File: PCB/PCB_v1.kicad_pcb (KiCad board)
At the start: 2 copper layers, 0 parts

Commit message: Accelerometer Footprint
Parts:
- added J1: Accelerometer, Stuffed Crust:Accelerometer, F.Cu at (179.4, 71.4)
- added J2: Flysky FS2A Receiver, Stuffed Crust:Flysky_FS2A_Receiver, F.Cu at (179.6, 94.1)
- added J3: DC-DC, Stuffed Crust:DC_DC, F.Cu at (137.0, 68.5)
- added J4: Battery Left, Stuffed Crust:Battery_or_LED, F.Cu at (98.2, 75.7)
- added J5: Battery Right, Stuffed Crust:Battery_or_LED, F.Cu at (212.0, 69.9)
- added J6: ESC Left, Stuffed Crust:ESC, F.Cu at (111.0, 91.5)
- added J7: ESC Right, Stuffed Crust:ESC, F.Cu at (214.0, 89.5)
- added J8: LED, Stuffed Crust:Battery_or_LED, F.Cu at (179.3, 61.3)
- added U1: Teensy4.0, Teensy:Teensy40, F.Cu at (164.1, 79.6)

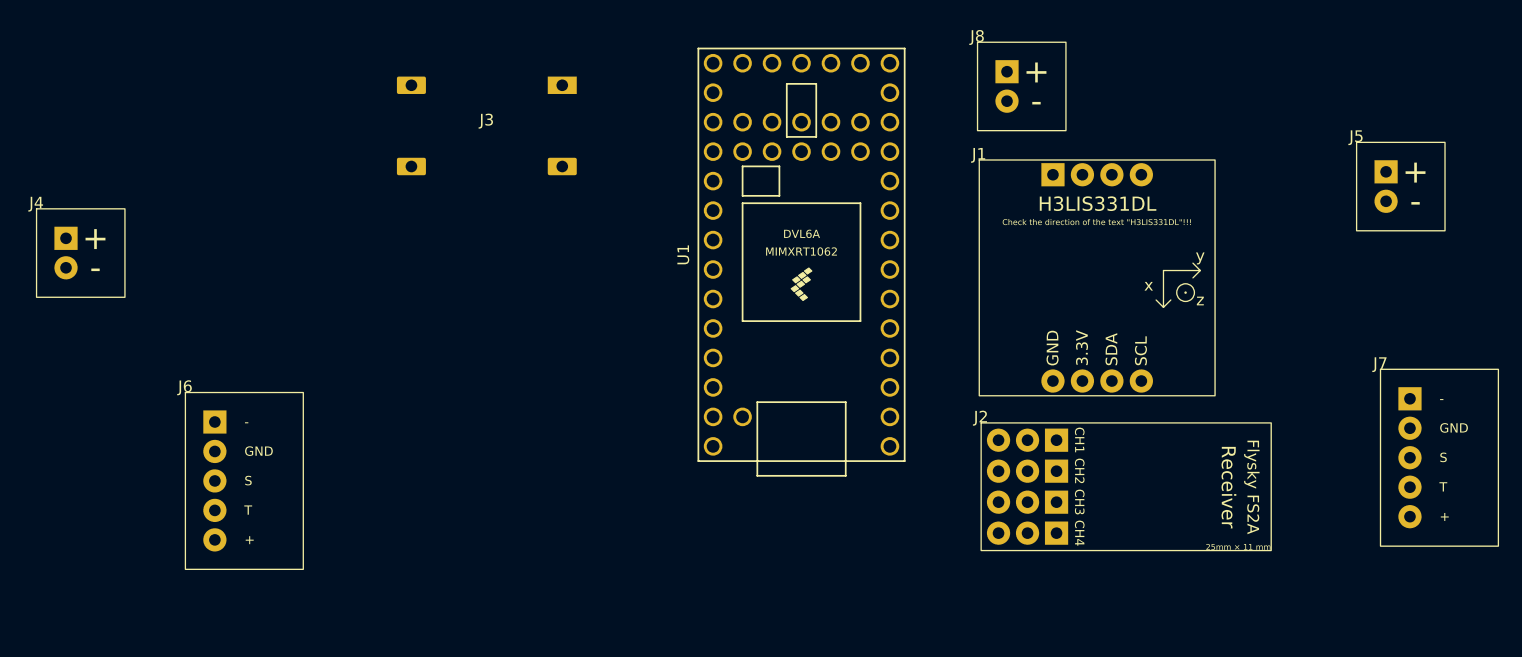
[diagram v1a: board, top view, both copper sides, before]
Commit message: Fix the layer issue in ESC footprint
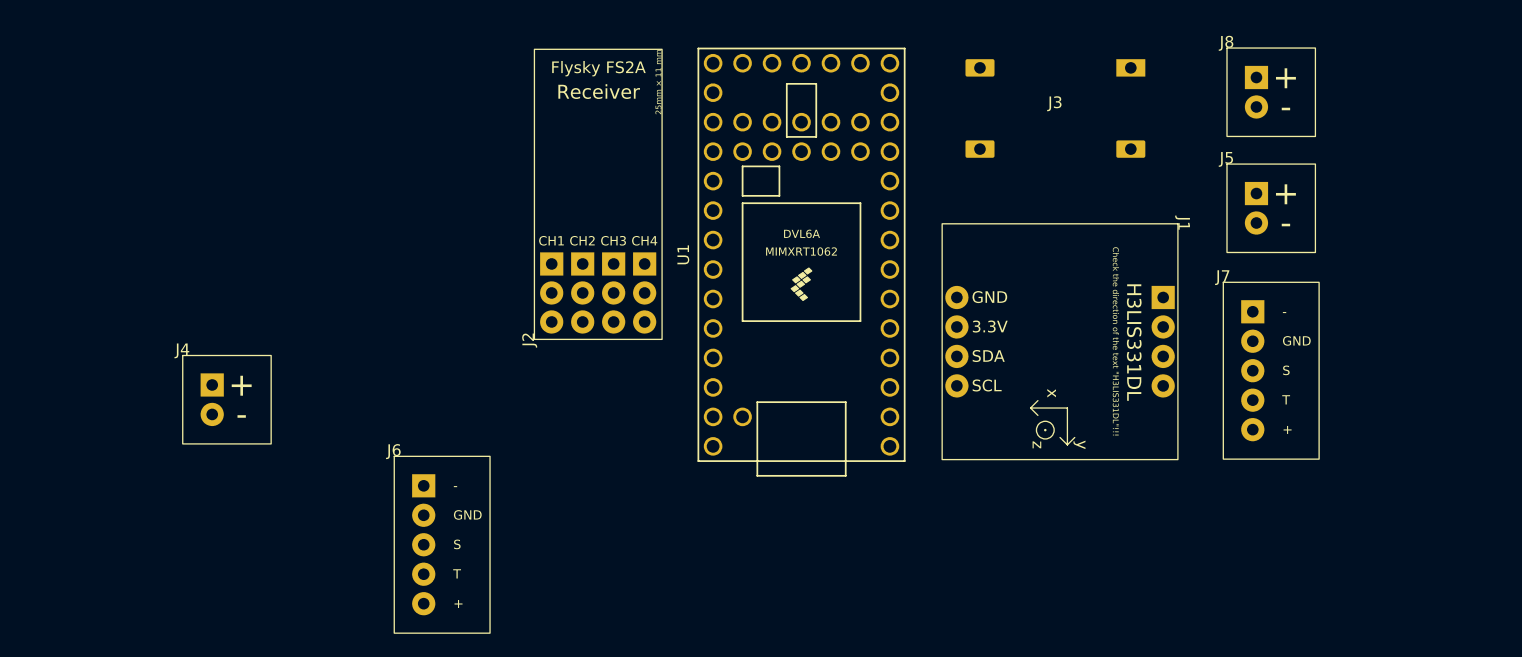
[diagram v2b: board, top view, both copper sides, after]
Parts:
- moved J3 49.0 mm to (186.0, 67.0)
- moved J2 39.2 mm to (141.1, 86.9), turned to 90 degrees
- moved J8 21.5 mm to (200.8, 61.8)
- moved J6 18.8 mm to (129.0, 97.0)
- moved J1 18.0 mm to (196.6, 76.9), turned to -90 degrees
- moved J4 17.8 mm to (110.8, 88.3)
- moved J7 15.5 mm to (200.5, 82.0)
- moved J5 11.3 mm to (200.8, 71.8)
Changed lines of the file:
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@@
 	(footprint "Stuffed Crust:Battery_or_LED"
 		(layer "F.Cu")
-		(at 179.29 61.29)
+		(at 200.79 61.79)
 		(property "Reference" "J8"
 			(at 0 -0.5 0)
@@
 	(footprint "Stuffed Crust:Battery_or_LED"
 		(layer "F.Cu")
-		(at 211.96 69.92)
+		(at 200.79 71.79)
 		(property "Reference" "J5"
 			(at 0 -0.5 0)
@@
 	(footprint "Stuffed Crust:DC_DC"
 		(layer "F.Cu")
-		(at 137 68.5)
+		(at 186 67)
 		(property "Reference" "J3"
 			(at 0 -0.5 0)
@@
 	(footprint "Stuffed Crust:ESC"
 		(layer "F.Cu")
-		(at 214.02 89.48)
+		(at 200.4725 81.98)
 		(property "Reference" "J7"
 			(at 0 -0.5 0)
@@
 		(fp_rect
 			(start 0 0)
-			(end 10.16 15.24)
+			(end 8.255 15.24)
 			(stroke
 				(width 0.1)
@@
 	(footprint "Stuffed Crust:Accelerometer"
 		(layer "F.Cu")
-		(at 179.44 71.44)
+		(at 196.56 76.94 -90)
 		(property "Reference" "J1"
-			(at 0 -0.5 0)
+			(at 0 -0.5 270)
 			(unlocked yes)
 			(layer "F.SilkS")
@@
 		)
 		(property "Value" "Accelerometer"
-			(at 0 1 0)
+			(at 0 1 270)
 			(unlocked yes)
 			(layer "F.Fab")
@@
 		)
 		(property "Datasheet" "~"
-			(at 0 0 0)
+			(at 0 0 270)
 			(unlocked yes)
 			(layer "F.Fab")
@@
 		)
 		(property "Description" "Generic connector, single row, 01x08, script generated"
-			(at 0 0 0)
+			(at 0 0 270)
 			(unlocked yes)
 			(layer "F.Fab")
@@
 		(sheetfile "PCB_v1.kicad_sch")
 		(fp_line
+			(start 15.875 12.7)
+			(end 15.24 12.065)
+			(stroke
+				(width 0.1)
+				(type default)
+			)
+			(layer "F.SilkS")
+		)
+		(fp_line
+			(start 15.875 12.7)
+			(end 16.51 12.065)
+			(stroke
+				(width 0.1)
+				(type default)
+			)
+			(layer "F.SilkS")
+		)
+		(fp_line
 			(start 15.875 9.525)
 			(end 15.875 12.7)
@@
 		)
 		(fp_line
-			(start 15.875 12.7)
-			(end 15.24 12.065)
-			(stroke
-				(width 0.1)
-				(type default)
-			)
-			(layer "F.SilkS")
-		)
-		(fp_line
-			(start 15.875 12.7)
-			(end 16.51 12.065)
+			(start 19.05 9.525)
+			(end 18.415 10.16)
 			(stroke
 				(width 0.1)
@@
 			(start 19.05 9.525)
 			(end 18.415 8.89)
-			(stroke
-				(width 0.1)
-				(type default)
-			)
-			(layer "F.SilkS")
-		)
-		(fp_line
-			(start 19.05 9.525)
-			(end 18.415 10.16)
 			(stroke
 				(width 0.1)
@@
 		)
 		(fp_text user "z"
-			(at 19.05 12.065 0)
+			(at 19.05 12.065 270)
 			(unlocked yes)
 			(layer "F.SilkS")
@@
 		)
 		(fp_text user "Check the direction of the text \"H3LIS331DL\"!!!"
-			(at 10.16 5.08 0)
+			(at 10.16 5.08 270)
 			(unlocked yes)
 			(layer "F.SilkS")
@@
 		)
 		(fp_text user "H3LIS331DL"
-			(at 10.16 3.81 0)
+			(at 10.16 3.81 270)
 			(unlocked yes)
 			(layer "F.SilkS")
@@
 		)
 		(fp_text user "SDA"
-			(at 11.43 17.78 90)
+			(at 11.43 17.78 0)
 			(unlocked yes)
 			(layer "F.SilkS")
@@
 		)
 		(fp_text user "SCL"
-			(at 13.97 17.78 90)
+			(at 13.97 17.78 0)
 			(unlocked yes)
 			(layer "F.SilkS")
@@
 		)
 		(fp_text user "3.3V"
-			(at 8.89 17.78 90)
+			(at 8.89 17.78 0)
 			(unlocked yes)
 			(layer "F.SilkS")
@@
 		)
 		(fp_text user "x"
-			(at 14.605 10.795 0)
+			(at 14.605 10.795 270)
 			(unlocked yes)
 			(layer "F.SilkS")
@@
 		)
 		(fp_text user "GND"
-			(at 6.35 17.78 90)
+			(at 6.35 17.78 0)
 			(unlocked yes)
 			(layer "F.SilkS")
@@
 		)
 		(fp_text user "y"
-			(at 19.05 8.255 0)
+			(at 19.05 8.255 270)
 			(unlocked yes)
 			(layer "F.SilkS")
@@
 		)
 		(fp_text user "${REFERENCE}"
-			(at 0 2.5 0)
+			(at 0 2.5 270)
 			(unlocked yes)
 			(layer "F.Fab")
@@
 		)
 		(pad "1" thru_hole rect
-			(at 6.35 1.27)
+			(at 6.35 1.27 270)
 			(size 2 2)
 			(drill 1)
@@
 		)
 		(pad "2" thru_hole roundrect
-			(at 8.89 1.27)
+			(at 8.89 1.27 270)
 			(size 2 2)
 			(drill 1)
@@
 		)
 		(pad "3" thru_hole roundrect
-			(at 11.43 1.27)
+			(at 11.43 1.27 270)
 			(size 2 2)
 			(drill 1)
@@
 		)
 		(pad "4" thru_hole roundrect
-			(at 13.97 1.27)
+			(at 13.97 1.27 270)
 			(size 2 2)
 			(drill 1)
@@
 		)
 		(pad "5" thru_hole roundrect
-			(at 6.35 19.05)
+			(at 6.35 19.05 270)
 			(size 2 2)
 			(drill 1)
@@
 		)
 		(pad "6" thru_hole roundrect
-			(at 8.89 19.05)
+			(at 8.89 19.05 270)
 			(size 2 2)
 			(drill 1)
@@
 		)
 		(pad "7" thru_hole roundrect
-			(at 11.43 19.05)
+			(at 11.43 19.05 270)
 			(size 2 2)
 			(drill 1)
@@
 		)
 		(pad "8" thru_hole roundrect
-			(at 13.97 19.05)
+			(at 13.97 19.05 270)
 			(size 2 2)
 			(drill 1)
@@
 	(footprint "Stuffed Crust:Flysky_FS2A_Receiver"
 		(layer "F.Cu")
-		(at 179.6 94.1)
+		(at 141.1 86.9 90)
 		(property "Reference" "J2"
-			(at 0 -0.5 0)
+			(at 0 -0.5 90)
 			(unlocked yes)
 			(layer "F.SilkS")
@@
 		)
 		(property "Value" "Flysky FS2A Receiver"
-			(at 0 1 0)
+			(at 0 1 90)
 			(unlocked yes)
 			(layer "F.Fab")
@@
 		)
 		(property "Datasheet" "~"
-			(at 0 0 0)
+			(at 0 0 90)
 			(unlocked yes)
 			(layer "F.Fab")
@@
 		)
 		(property "Description" "Generic connector, single row, 01x12, script generated"
-			(at 0 0 0)
+			(at 0 0 90)
 			(unlocked yes)
 			(layer "F.Fab")
@@
 		)
 		(fp_text user "Receiver"
-			(at 22 5.5 270)
+			(at 22 5.5 0)
 			(unlocked yes)
 			(layer "F.SilkS")
@@
 		)
 		(fp_text user "CH2"
-			(at 8 4.16 270)
+			(at 8 4.16 0)
 			(unlocked yes)
 			(layer "F.SilkS")
@@
 		)
 		(fp_text user "CH1"
-			(at 8 1.49 270)
+			(at 8 1.49 0)
 			(unlocked yes)
 			(layer "F.SilkS")
@@
 		)
 		(fp_text user "CH3"
-			(at 8 6.83 270)
+			(at 8 6.83 0)
 			(unlocked yes)
 			(layer "F.SilkS")
@@
 		)
 		(fp_text user "Flysky FS2A"
-			(at 24 5.5 270)
+			(at 24 5.5 0)
 			(unlocked yes)
 			(layer "F.SilkS")
@@
 		)
 		(fp_text user "CH4"
-			(at 8 9.5 270)
+			(at 8 9.5 0)
 			(unlocked yes)
 			(layer "F.SilkS")
@@
 		)
 		(fp_text user "25mm × 11 mm"
-			(at 25 11 0)
+			(at 25 11 90)
 			(unlocked yes)
 			(layer "F.SilkS")
@@
 		)
 		(fp_text user "${REFERENCE}"
-			(at 0 2.5 0)
+			(at 0 2.5 90)
 			(unlocked yes)
 			(layer "F.Fab")
@@
 		)
 		(pad "1" thru_hole rect
-			(at 6.5 1.49)
+			(at 6.5 1.49 90)
 			(size 2 2)
 			(drill 1)
@@
 		)
 		(pad "2" thru_hole rect
-			(at 6.5 4.16)
+			(at 6.5 4.16 90)
 			(size 2 2)
 			(drill 1)
@@
 		)
 		(pad "3" thru_hole rect
-			(at 6.5 6.83)
+			(at 6.5 6.83 90)
 			(size 2 2)
 			(drill 1)
@@
 		)
 		(pad "4" thru_hole rect
-			(at 6.5 9.5)
+			(at 6.5 9.5 90)
 			(size 2 2)
 			(drill 1)
@@
 		)
 		(pad "5" thru_hole circle
-			(at 4 1.49)
+			(at 4 1.49 90)
 			(size 2 2)
 			(drill 1)
@@
 		)
 		(pad "6" thru_hole circle
-			(at 4 4.16)
+			(at 4 4.16 90)
 			(size 2 2)
 			(drill 1)
@@
 		)
 		(pad "7" thru_hole circle
-			(at 4 6.83)
+			(at 4 6.83 90)
 			(size 2 2)
 			(drill 1)
@@
 		)
 		(pad "8" thru_hole circle
-			(at 4 9.5)
+			(at 4 9.5 90)
 			(size 2 2)
 			(drill 1)
@@
 		)
 		(pad "9" thru_hole circle
-			(at 1.5 1.49)
+			(at 1.5 1.49 90)
 			(size 2 2)
 			(drill 1)
@@
 		)
 		(pad "10" thru_hole circle
-			(at 1.5 4.16)
+			(at 1.5 4.16 90)
 			(size 2 2)
 			(drill 1)
@@
 		)
 		(pad "11" thru_hole circle
-			(at 1.5 6.83)
+			(at 1.5 6.83 90)
 			(size 2 2)
 			(drill 1)
@@
 		)
 		(pad "12" thru_hole circle
-			(at 1.5 9.5)
+			(at 1.5 9.5 90)
 			(size 2 2)
 			(drill 1)
@@
 	(footprint "Stuffed Crust:Battery_or_LED"
 		(layer "F.Cu")
-		(at 98.19 75.65)
+		(at 110.79 88.29)
 		(property "Reference" "J4"
 			(at 0 -0.5 0)
@@
 	(footprint "Stuffed Crust:ESC"
 		(layer "F.Cu")
-		(at 111.02 91.48)
+		(at 129.02 96.98)
 		(property "Reference" "J6"
 			(at 0 -0.5 0)
@@
 		(fp_rect
 			(start 0 0)
-			(end 10.16 15.24)
-			(stroke
-				(width 0.1)
+			(end 8.255 15.24)
+			(stroke
+				(width 0.1)

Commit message: Put components onto PCB
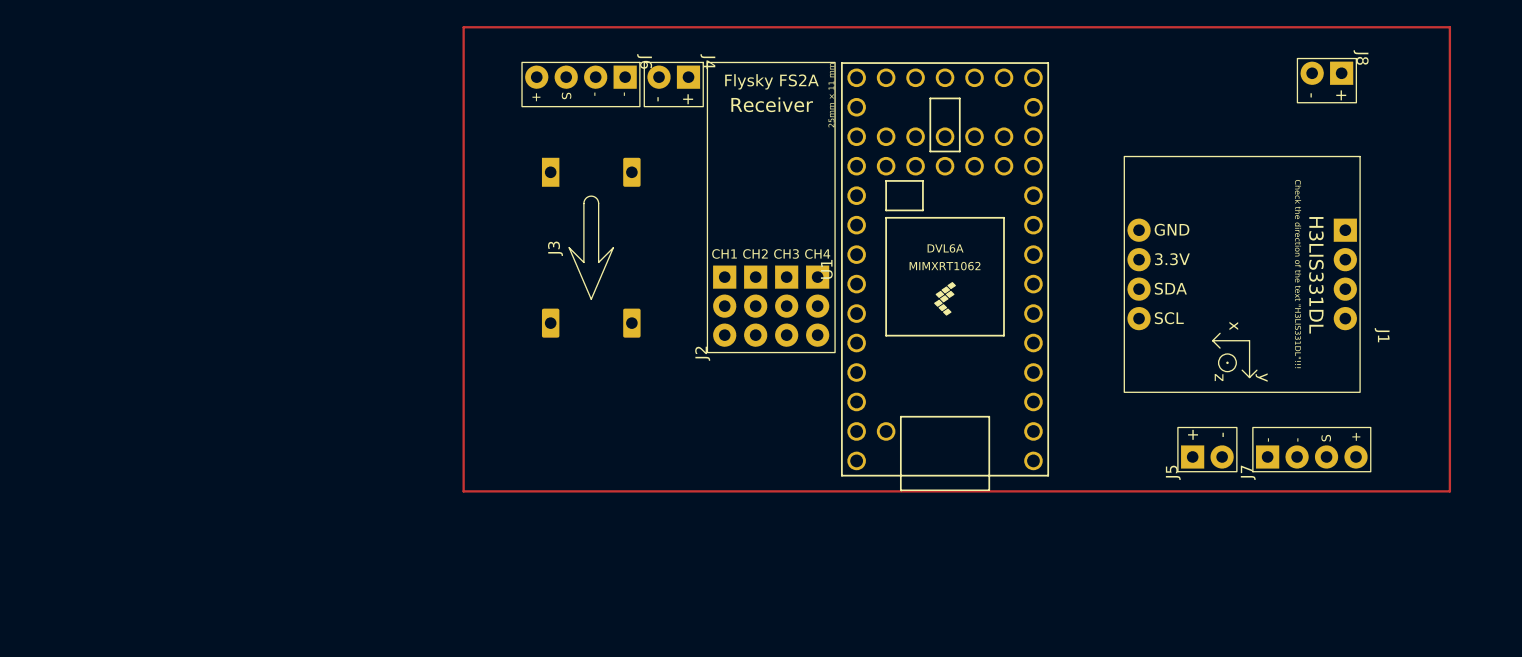
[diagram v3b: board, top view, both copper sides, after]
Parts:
- J6: value ESC Left -> ESC_Left
- J7: value ESC Right -> ESC_Right
- moved J4 51.5 mm to (155.7, 63.0), turned to -90 degrees
- moved J3 41.8 mm to (146.0, 79.0), turned to 90 degrees
- moved J6 40.0 mm to (150.2, 63.0), turned to -90 degrees
- moved J5 26.9 mm to (196.6, 98.3), turned to 90 degrees
- moved J1 16.7 mm to (212.3, 71.1)
- moved J7 16.5 mm to (203.0, 98.3), turned to 90 degrees
- moved J2 15.0 mm to (156.0, 88.0)
- moved U1 12.4 mm to (176.5, 80.9)
- moved J8 11.2 mm to (211.9, 62.7), turned to -90 degrees
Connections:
- J6 pad 4: unconnected-(J6-Pin_4-Pad4) -> /12V
- J7 pad 4: unconnected-(J7-Pin_4-Pad4) -> /12V

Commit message: Fix DC_DC Footprint
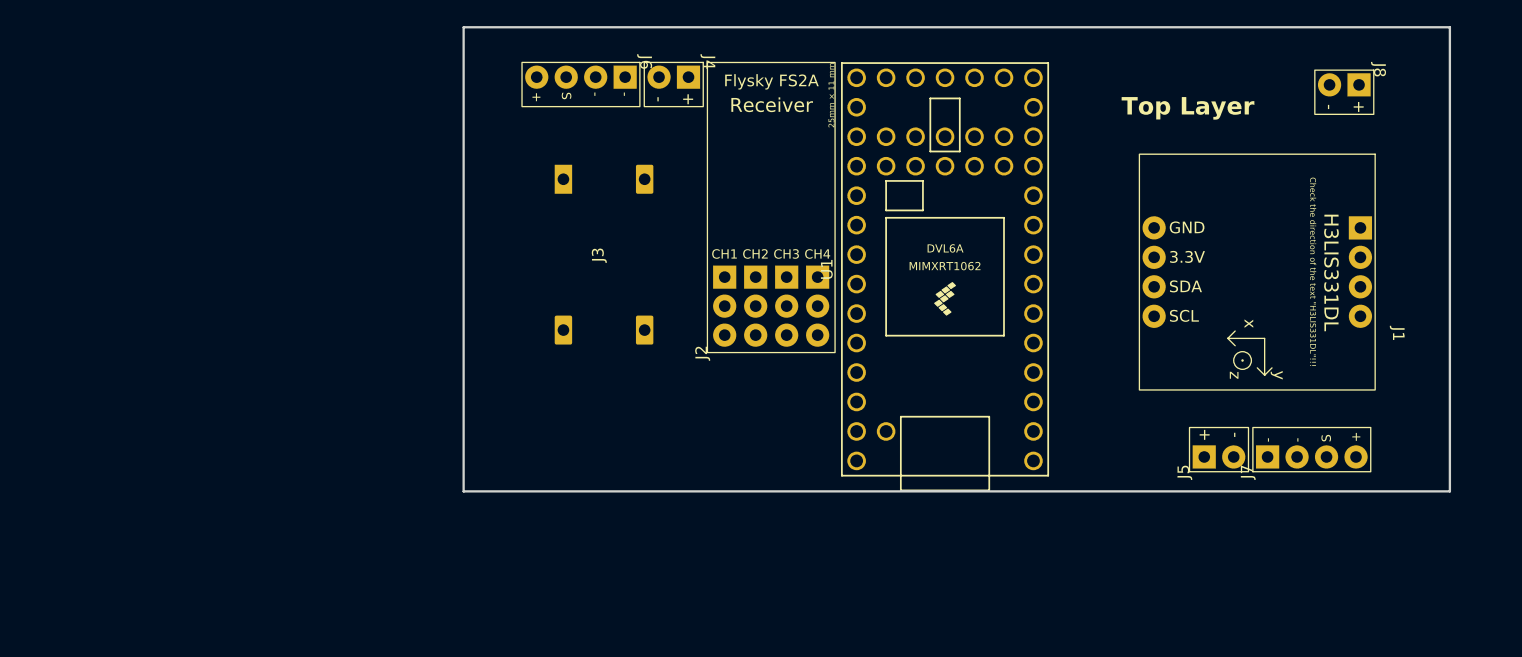
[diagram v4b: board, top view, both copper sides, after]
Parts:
- moved J8 1.80 mm to (213.4, 63.7)
- moved J1 1.32 mm to (213.6, 70.9)
- moved J3 1.25 mm to (147.1, 79.6)
- moved J5 1.00 mm to (197.6, 98.3)
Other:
- board outline added: 85 x 40 mm
- board text added: "Top Layer"

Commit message: Put DC_DC back to the front layer; change the PCB layout
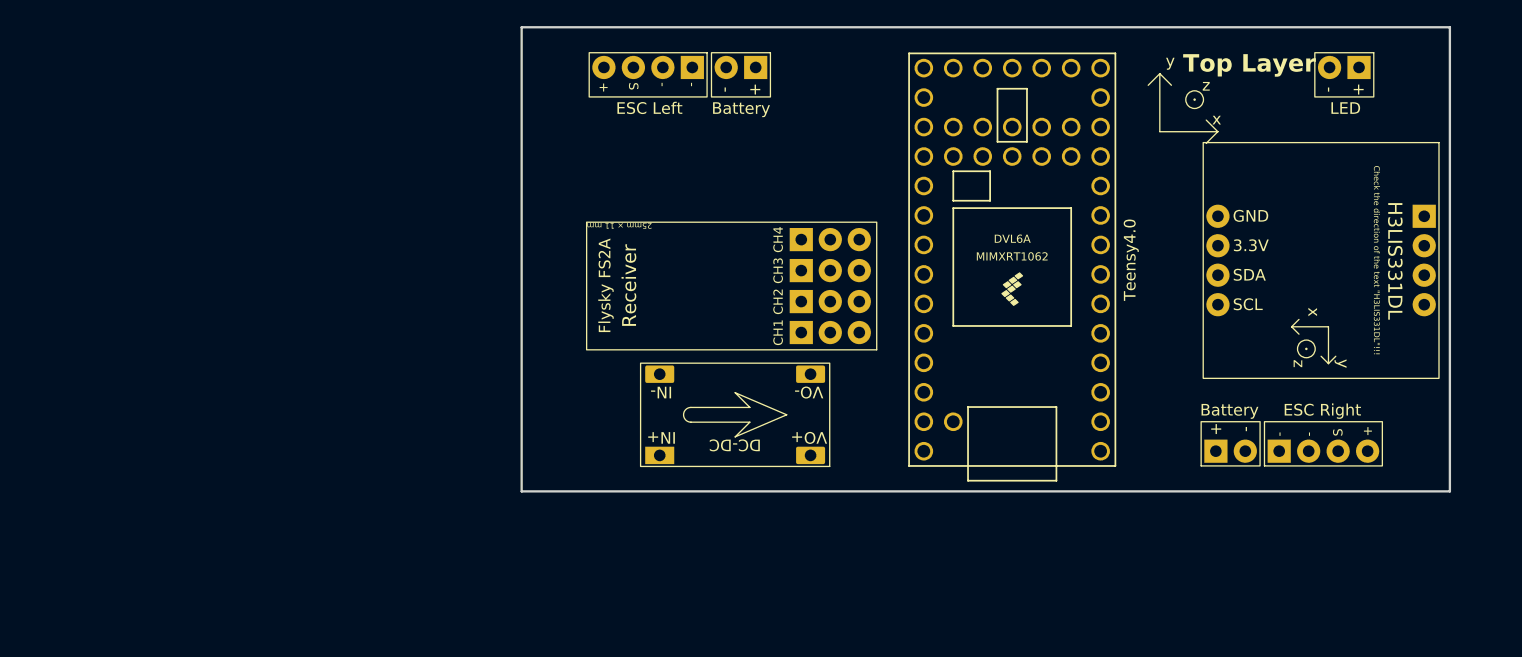
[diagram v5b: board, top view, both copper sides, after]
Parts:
- added ?: , clipboard:2c392293-ef90-46e6-a046-d4cdf45f70c2, F.Cu at (198.0, 67.0)
- added ?: , clipboard:1efe44ad-3118-4d5e-9bd0-140298458513, F.Cu at (199.0, 65.0)
- moved J3 17.8 mm to (158.4, 93.4), turned to 180 degrees
- moved J2 14.6 mm to (170.6, 87.8), turned to 180 degrees
- moved J4 5.85 mm to (161.4, 62.2)
- moved J6 5.85 mm to (156.0, 62.2)
- moved U1 5.85 mm to (182.3, 80.0)
- moved J1 5.59 mm to (219.1, 69.9)
- moved Je 1.50 mm to (213.4, 62.2)
- moved J5 1.12 mm to (198.6, 97.8)
- moved J7 1.12 mm to (204.0, 97.8)
- renumbered J8 to Je
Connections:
- J3 pad 1: /GND -> /12V
- J3 pad 2: /12V -> /GND
- J3 pad 3: /GND -> /5V
- J3 pad 4: /5V -> /GND
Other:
- board size 85 x 40 mm -> 80 x 40 mm
- board text added: "Battery"
- board text added: "ESC Left"
- board text added: "ESC Right"
- board text added: "LED"
- board text added: "x"
- board text added: "y"

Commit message: PCB Finished
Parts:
- moved ? 29.2 mm to (168.9, 64.8)
- moved ? 29.2 mm to (169.9, 62.8)
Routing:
- net /12V: track 0.00 -> 123.9 mm
- net /S_ESC_Left_2: track 0.00 -> 61.5 mm
- net /3.3V: track 0.00 -> 60.4 mm
- net /S_ESC_Right_3: track 0.00 -> 29.0 mm
- net /SDA_18: track 0.00 -> 27.5 mm
- net /SCL_19: track 0.00 -> 27.5 mm
- net /LED: track 0.00 -> 24.1 mm
- net /CH4_20: track 0.00 -> 11.8 mm
- net /CH3_21: track 0.00 -> 11.7 mm
- net /CH2_22: track 0.00 -> 11.7 mm
- net /CH1_23: track 0.00 -> 11.6 mm
- net /5V: track 0.00 -> 9.91 mm
- added copper zone on B.Cu, net /GND
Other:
- board text added: "Bottom Layer"
- board text added: "Stuffed Crust"
- board text added: "Wildcat Robotics"
